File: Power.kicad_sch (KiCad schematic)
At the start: 8 parts, among them J100 5V Input, U100 ADP3330ARTZ3.3-RL7

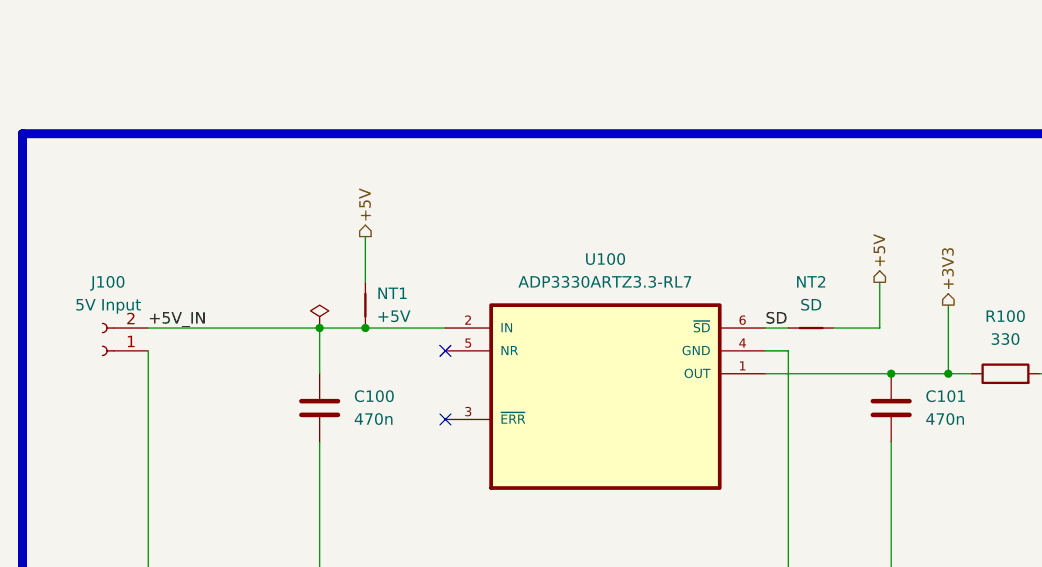
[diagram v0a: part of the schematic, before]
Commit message: [pcb][changed] updated footprints that were incorrect, changed flash memory module due to stock issues
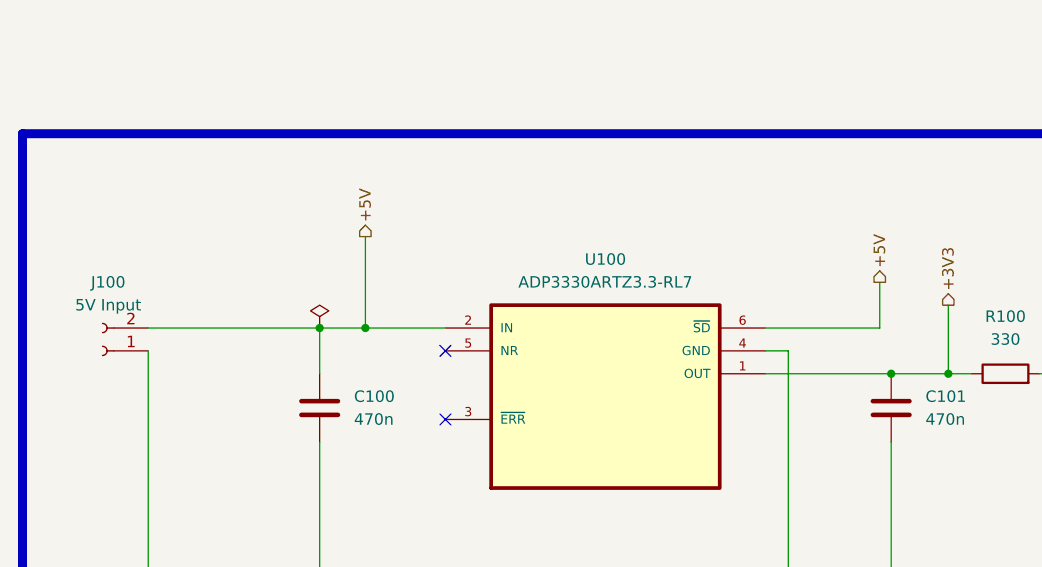
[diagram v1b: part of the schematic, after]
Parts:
- removed NT1: +5V, symbol Device:NetTie_2
- removed NT2: SD, symbol Device:NetTie_2
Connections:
- net +5V_IN is gone; now on net +5V: C100.1, J100.2 (Pin_2), U100.2 (IN)
- net SD is gone; now on net +5V: U100.6 (~{SD})
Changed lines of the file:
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@@
+	)
+	(junction
+		(at 116.84 85.09)
+		(diameter 0)
+		(color 0 0 0 0)
 	)
 	(junction
@@
 		(color 0 0 0 0)
 	)
-	(junction
-		(at 116.84 85.09)
-		(diameter 0)
-		(color 0 0 0 0)
-	)
 	(no_connect
 		(at 125.73 87.63)
@@
 	(wire
 		(pts
-			(xy 168.91 85.09) (xy 173.99 85.09)
-		)
-		(stroke
-			(width 0)
-			(type default)
-		)
-	)
-	(wire
-		(pts
-			(xy 116.84 74.93) (xy 116.84 80.01)
+			(xy 116.84 74.93) (xy 116.84 85.09)
 		)
 		(stroke
@@
 	(wire
 		(pts
+			(xy 116.84 85.09) (xy 125.73 85.09)
+		)
+		(stroke
+			(width 0)
+			(type default)
+		)
+	)
+	(wire
+		(pts
 			(xy 111.76 97.79) (xy 111.76 116.84)
 		)
@@
 	(wire
 		(pts
-			(xy 116.84 85.09) (xy 125.73 85.09)
+			(xy 111.76 85.09) (xy 116.84 85.09)
 		)
 		(stroke
@@
 	(wire
 		(pts
-			(xy 163.83 85.09) (xy 161.29 85.09)
-		)
-		(stroke
-			(width 0)
-			(type default)
-		)
-	)
-	(wire
-		(pts
-			(xy 111.76 85.09) (xy 116.84 85.09)
+			(xy 161.29 85.09) (xy 173.99 85.09)
 		)
 		(stroke
@@
 			(width 0)
 			(type default)
-		)
-	)
-	(label "SD"
-		(at 161.29 85.09 0)
-		(effects
-			(font
-				(size 1.27 1.27)
-			)
-			(justify left bottom)
-		)
-	)
-	(label "+5V_IN"
-		(at 92.71 85.09 0)
-		(effects
-			(font
-				(size 1.27 1.27)
-			)
-			(justify left bottom)
 		)
 	)
@@
 			)
 			(justify left)
-		)
-	)
-	(netclass_flag ""
-		(length 2.54)
-		(shape round)
-		(at 101.6 85.09 0)
-		(effects
-			(font
-				(size 1.27 1.27)
-			)
-			(justify left bottom)
-		)
-		(property "Netclass" "Power 5V"
-			(at 97.79 80.772 0)
-			(effects
-				(font
-					(size 1.27 1.27)
-				)
-				(justify left)
-			)
-		)
-		(property "Component Class" ""
-			(at -77.47 2.54 0)
-			(effects
-				(font
-					(size 1.27 1.27)
-					(italic yes)
-				)
-			)
 		)
 	)
@@
 					(unit 1)
 				)
-			)
-		)
-	)
-	(symbol
-		(lib_id "Device:NetTie_2")
-		(at 116.84 82.55 90)
-		(unit 1)
-		(exclude_from_sim no)
-		(in_bom no)
-		(on_board yes)
-		(dnp no)
-		(fields_autoplaced yes)
-		(property "Reference" "NT1"
-			(at 118.11 81.2799 90)
-			(effects
-				(font
-					(size 1.27 1.27)
-				)
-				(justify right)
-			)
-		)
-		(property "Value" "+5V"
-			(at 118.11 83.8199 90)
-			(effects
-				(font
-					(size 1.27 1.27)
-				)
-				(justify right)
-			)
-		)
-		(property "Footprint" ""
-			(at 116.84 82.55 0)
-			(effects
-				(font
-					(size 1.27 1.27)
-				)
-				(hide yes)
-			)
-		)
-		(property "Datasheet" "~"
-			(at 116.84 82.55 0)
-			(effects
-				(font
-					(size 1.27 1.27)
-				)
-				(hide yes)
-			)
-		)
-		(property "Description" "Net tie, 2 pins"
-			(at 116.84 82.55 0)
-			(effects
-				(font
-					(size 1.27 1.27)
-				)
-				(hide yes)
-			)
-		)
-		(pin "2"
-		)
-		(pin "1"
-		)
-		(instances
-			(project "DumbFCC"
-				(path "/f9e05184-c88b-4a88-ae9c-ab2bdb32be7c/c5103ceb-5325-4a84-a025-9638a412984e/58f06ef5-dfdb-4ead-843d-bbbaac634f9b"
-					(reference "NT1")
-					(unit 1)
-				)
-			)
-		)
-	)
-	(symbol
-		(lib_id "Device:NetTie_2")
-		(at 166.37 85.09 0)
-		(unit 1)
-		(exclude_from_sim no)
-		(in_bom no)
-		(on_board yes)
-		(dnp no)
-		(fields_autoplaced yes)
-		(property "Reference" "NT2"
-			(at 166.37 80.01 0)
-			(effects
-				(font
-					(size 1.27 1.27)
-				)
-			)
-		)
-		(property "Value" "SD"
-			(at 166.37 82.55 0)
-			(effects
-				(font
-					(size 1.27 1.27)
-				)
-			)
-		)
-		(property "Footprint" ""
-			(at 166.37 85.09 0)
-			(effects
-				(font
-					(size 1.27 1.27)
-				)
-				(hide yes)
-			)
-		)
-		(property "Datasheet" "~"
-			(at 166.37 85.09 0)
-			(effects
-				(font
-					(size 1.27 1.27)
-				)
-				(hide yes)
-			)
-		)
-		(property "Description" "Net tie, 2 pins"
-			(at 166.37 85.09 0)
-			(effects
-				(font
-					(size 1.27 1.27)
-				)
-				(hide yes)
-			)
-		)
-		(pin "2"
-		)
-		(pin "1"
-		)
-		(instances
-			(project "DumbFCC"
-				(path "/f9e05184-c88b-4a88-ae9c-ab2bdb32be7c/c5103ceb-5325-4a84-a025-9638a412984e/58f06ef5-dfdb-4ead-843d-bbbaac634f9b"
-					(reference "NT2")
-					(unit 1)
-				)
